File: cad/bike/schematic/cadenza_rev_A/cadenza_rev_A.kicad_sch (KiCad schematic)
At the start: 49 parts, among them J1 USB_A, J2 USB_C_Receptacle, J3 Conn_01x02, J4 Conn_01x02, Q1 BC547, U1 TLC5916, U10 HDSP-A151, U11 TLC5916, U12 HDSP-A151, U13 STM32F105RCTx, U15 TLC5916, U2 HDSP-A151, U3 TLC5916, U4 HDSP-A151, U5 TLC5916, U6 HDSP-A151, U7 TLC5916, U8 HDSP-A151, U9 TLC5916

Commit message: added the 3.3V LDO + switches + push buttons
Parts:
- added C13: 10nF, Capacitor_SMD:C_0805_2012Metric_Pad1.18x1.45mm_HandSolder, symbol Device:C
- added D10: LED, LED_THT:LED_D3.0mm, symbol Device:LED
- added H1, H2, H3, H4: MountingHole_Pad, MountingHole:MountingHole_3.2mm_M3_Pad_Via, symbol Mechanical:MountingHole_Pad
- added J5: Conn_01x02, Connector_PinHeader_2.54mm:PinHeader_1x02_P2.54mm_Vertical, symbol Connector_Generic:Conn_01x02
- added R11, R7: R_US, Resistor_SMD:R_0805_2012Metric_Pad1.20x1.40mm_HandSolder, symbol Device:R_US
- added SW1: SW_Slide_DPDT, Button_Switch_THT:SW_NKK_GW12LJP, symbol Switch:SW_Slide_DPDT
- added SW2, SW3: SW_Push, Button_Switch_SMD:SW_Push_1P1T_NO_CK_KSC6xxG, symbol Switch:SW_Push
- added U14: LT1962-3.3, Package_SO:MSOP-8_3x3mm_P0.65mm, symbol Regulator_Linear:LT1962-3.3
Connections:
- net +3.3V: now also C13.1, J5.1 (Pin_1), U14.1 (OUT), U14.2 (SENSE)
- net +5V: now also R11.1, U14.5 (~{SHDN}), U14.8 (IN)
- net GND: now also J2.S1 (SHIELD), D10.1 (K), H1.1, H2.1, H3.1, H4.1, R7.2, U14.4 (GND)
- net at J2.A4 (VBUS), J2.A9 (VBUS), J2.B4 (VBUS)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: now also SW1.2 (B); no longer J4.1 (Pin_1)
- new net: J4.1 (Pin_1), SW1.3 (C)
- new net: C13.2, U14.3 (BYP)
- new net: J5.2 (Pin_2), R7.1
- new net: D10.2 (A), R11.2
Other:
- moved on the sheet: C1, C10, C11, C2, C9, D9, J1, J2, J4, R5, U13

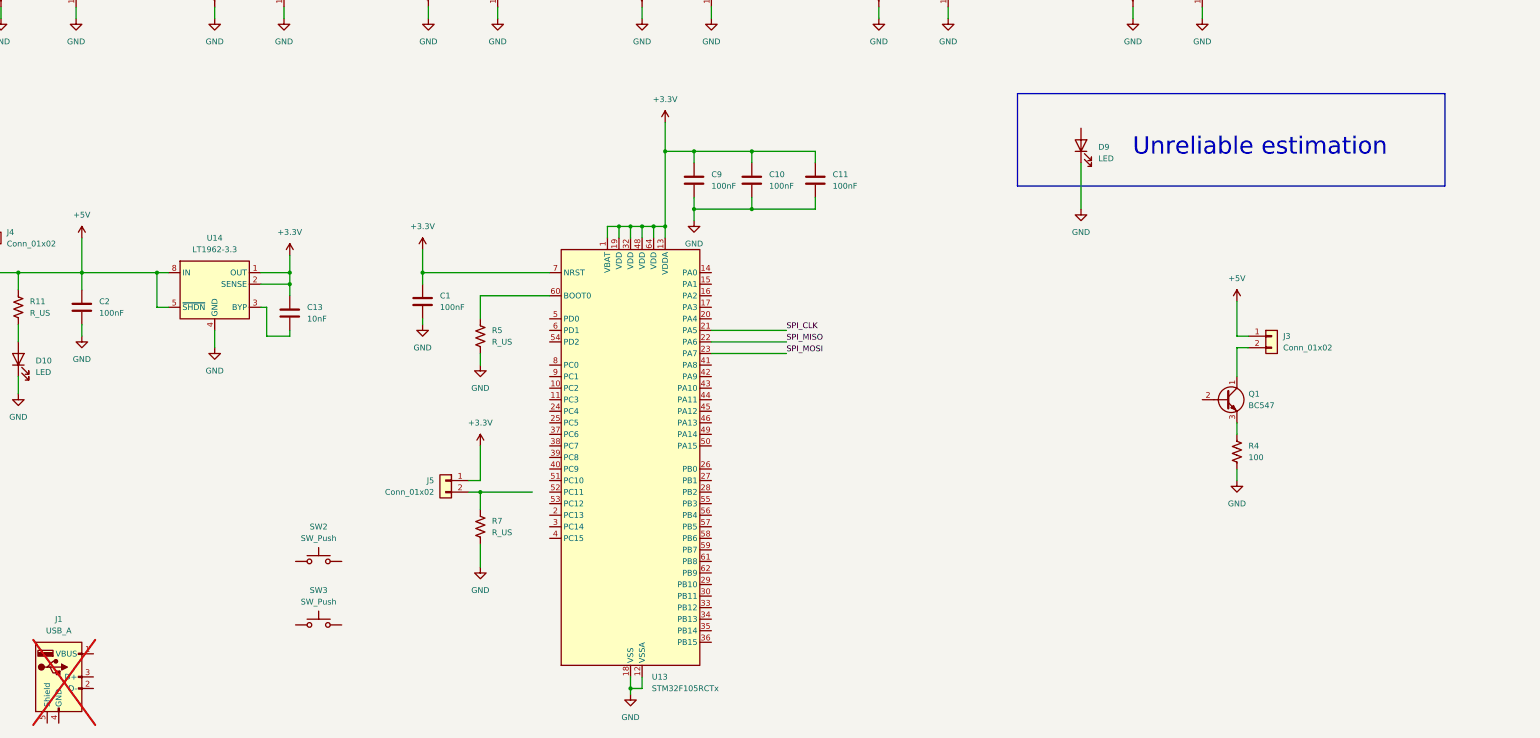
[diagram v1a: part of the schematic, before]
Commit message: added the debug interface
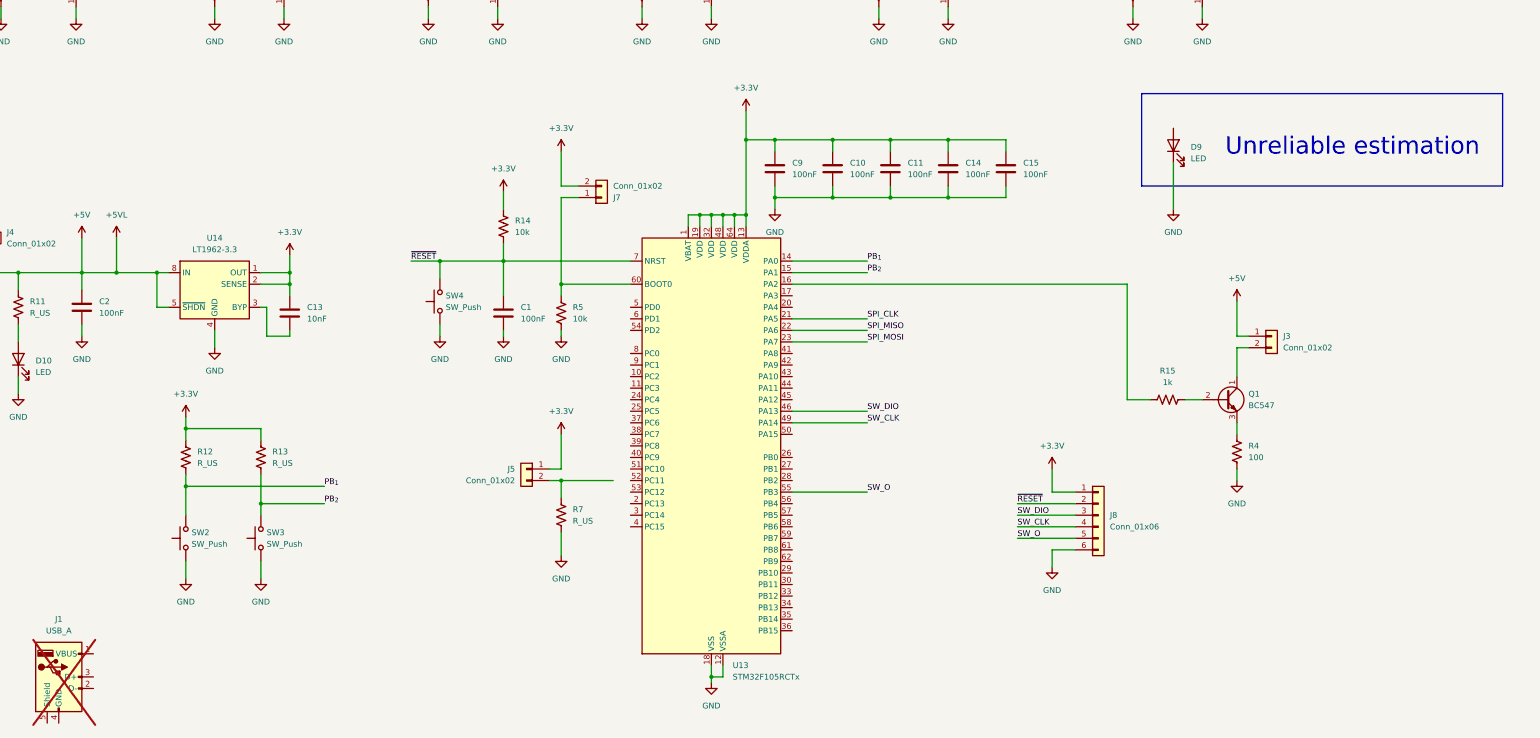
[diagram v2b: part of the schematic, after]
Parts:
- added C14, C15: 100nF, Capacitor_SMD:C_0805_2012Metric_Pad1.18x1.45mm_HandSolder, symbol Device:C
- added J7: Conn_01x02, Connector_PinHeader_2.54mm:PinHeader_1x02_P2.54mm_Vertical, symbol Connector_Generic:Conn_01x02
- added J8: Conn_01x06, Connector_PinHeader_2.54mm:PinHeader_1x06_P2.54mm_Vertical, symbol Connector_Generic:Conn_01x06
- added R12, R13: R_US, Resistor_SMD:R_0805_2012Metric_Pad1.20x1.40mm_HandSolder, symbol Device:R_US
- added R14: 10k, Resistor_SMD:R_0805_2012Metric_Pad1.20x1.40mm_HandSolder, symbol Device:R_US
- added R15: 1k, Resistor_SMD:R_0805_2012Metric_Pad1.20x1.40mm_HandSolder, symbol Device:R_US
- added SW4: SW_Push, Button_Switch_SMD:SW_Push_1P1T_NO_CK_KSC6xxG, symbol Switch:SW_Push
- R5: value R_US -> 10k
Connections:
- net +5VL is gone; now on net +5V: D1.2 (A), D2.2 (A), D3.2 (A), D4.2 (A), D5.2 (A), D6.2 (A), D7.2 (A), D8.2 (A), U10.1 (CA), U10.6 (CA), U12.1 (CA), U12.6 (CA), U2.1 (CA), U2.6 (CA), U4.1 (CA), U4.6 (CA), U6.1 (CA), U6.6 (CA), U8.1 (CA), U8.6 (CA)
- net +3.3V: now also C14.1, C15.1, J7.2 (Pin_2), J8.1 (Pin_1), R12.1, R13.1, R14.1; no longer C1.1, U13.7 (NRST)
- net GND: now also SW2.1, SW3.1, C14.2, C15.2, J8.6 (Pin_6), SW4.1
- net PB_{2}: now reaches SW3.2
- net PB_{2}: now also U13.15 (PA1), R13.2
- net PB_{1}: now reaches U13.14 (PA0)
- net PB_{1}: now also SW2.2, R12.2
- net at U13.16 (PA2): now also R15.1
- net SW_DIO: now reaches U13.46 (PA13)
- net SW_DIO: now also J8.3 (Pin_3)
- net SW_CLK: now reaches U13.49 (PA14)
- net SW_CLK: now also J8.4 (Pin_4)
- net SW_O: now reaches U13.55 (PB3)
- net SW_O: now also J8.5 (Pin_5)
- net at R5.1, U13.60 (BOOT0): now also J7.1 (Pin_1)
- net at Q1.2 (B): now also R15.2
- new net ~{RESET}: C1.1, J8.2 (Pin_2), R14.2, SW4.2, U13.7 (NRST)
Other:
- moved on the sheet: C1, C10, C11, C9, D9, J5, R5, R7, SW2, SW3, U13

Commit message: routing backup
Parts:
- added C16, C17, C18, C19: 100nF, Capacitor_SMD:C_0805_2012Metric_Pad1.18x1.45mm_HandSolder, symbol Device:C
- added R16: 330, Resistor_SMD:R_0805_2012Metric_Pad1.20x1.40mm_HandSolder, symbol Device:R_US
- R12, R13, R7: value R_US -> 4.7k
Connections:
- net +3.3V: now also R7.1, C19.1; no longer J5.1 (Pin_1)
- net GND: now also C16.2, C17.2, C18.2, C19.2; no longer R7.2
- net PB_{1}: now also C16.1
- net PB_{2}: now also C17.1
- net at J2.A4 (VBUS), J2.A9 (VBUS), J2.B4 (VBUS)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: now also SW1.5 (B); no longer SW1.2 (B)
- net at SW1.3 (C): no longer J4.1 (Pin_1)
- net at SW1.6 (C): now also J4.1 (Pin_1)
- net ~{LED_OUTPUT_EN}: now reaches U1.13 (~{OE}(ED2)), U11.13 (~{OE}(ED2)), U15.13 (~{OE}(ED2)), U3.13 (~{OE}(ED2)), U5.13 (~{OE}(ED2)), U7.13 (~{OE}(ED2)), U9.13 (~{OE}(ED2))
- net ~{LED_OUTPUT_EN}: now also U13.35 (PB14)
- net LED_LATCH_EN: now reaches U1.4 (LE(ED1)), U11.4 (LE(ED1)), U15.4 (LE(ED1)), U3.4 (LE(ED1)), U5.4 (LE(ED1)), U7.4 (LE(ED1)), U9.4 (LE(ED1))
- net LED_LATCH_EN: now also U13.20 (PA4)
- net WARNING_LED: now reaches U13.33 (PB12)
- net WARNING_LED: now also R16.1
- net at U13.40 (PC9): now also J5.2 (Pin_2), C18.1
- net at D9.2 (A): now also R16.2
- new net: J5.1 (Pin_1), R7.2
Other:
- note added: "sensor input"
- moved on the sheet: C12, C3, C4, C5, C6, C7, C8, D1, D2, D3, D4, D5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

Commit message: added final touches, no more nets to route
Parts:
- added TP1, TP2, TP3, TP4, TP5: TestPoint, TestPoint:TestPoint_Pad_D1.0mm, symbol Connector:TestPoint
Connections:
- net LED_LATCH_EN: now also TP3.1
- net SPI_CLK: now also TP1.1
- net SPI_MISO: now also TP5.1
- net SPI_MOSI: now also TP2.1
- net ~{LED_OUTPUT_EN}: now also TP4.1
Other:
- moved on the sheet: SW1

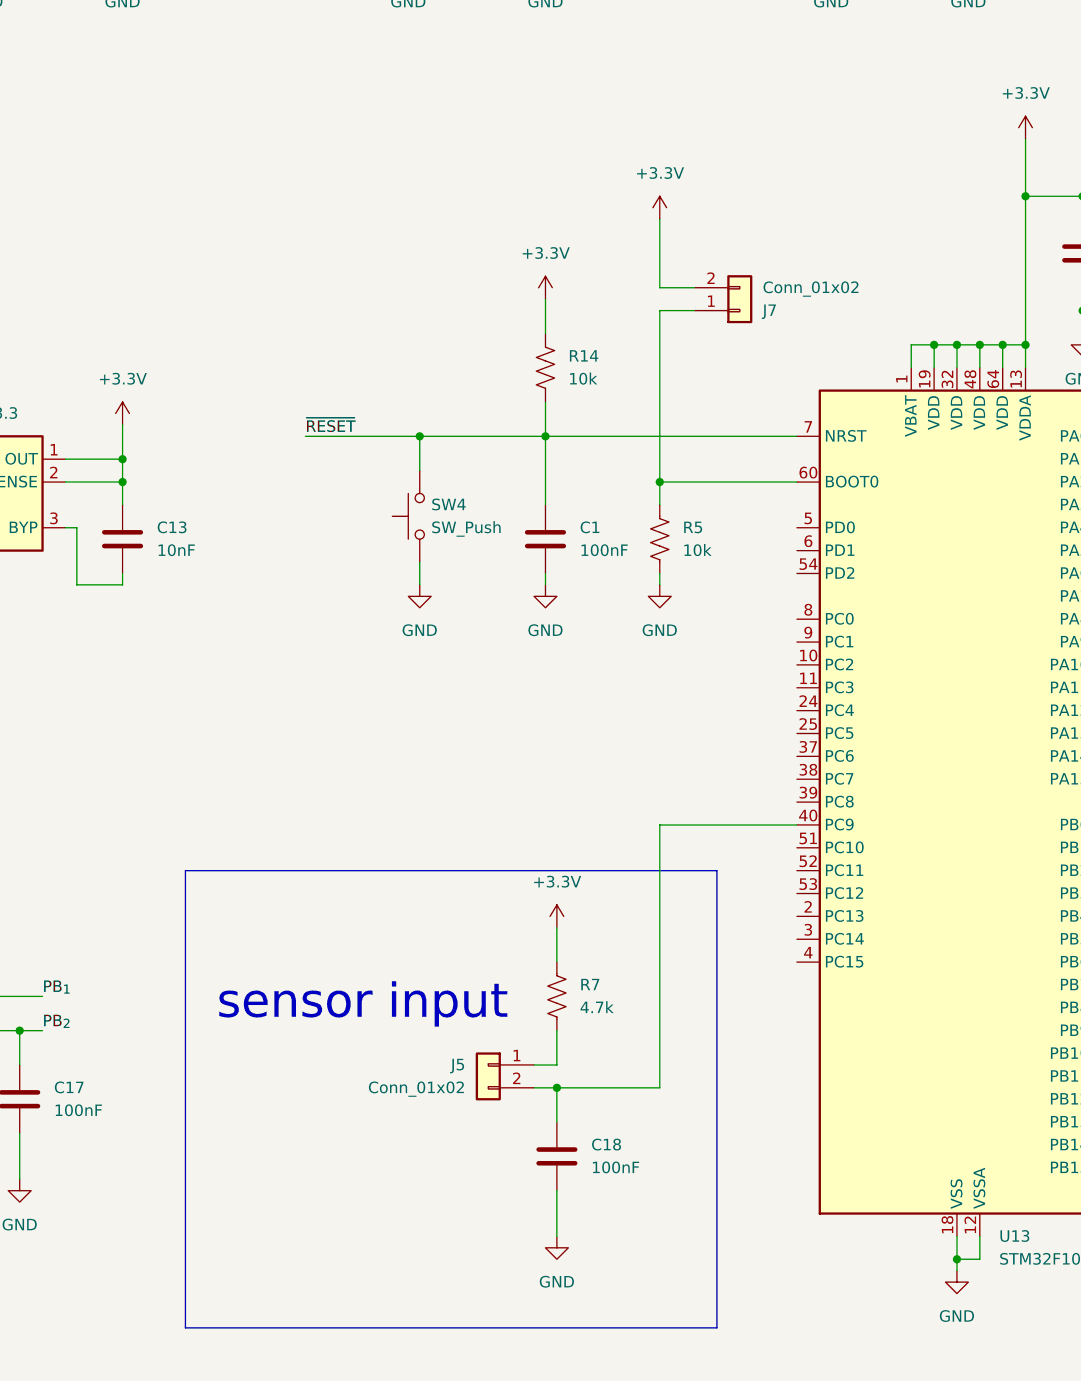
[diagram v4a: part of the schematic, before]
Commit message: added schematic added software pinout definition
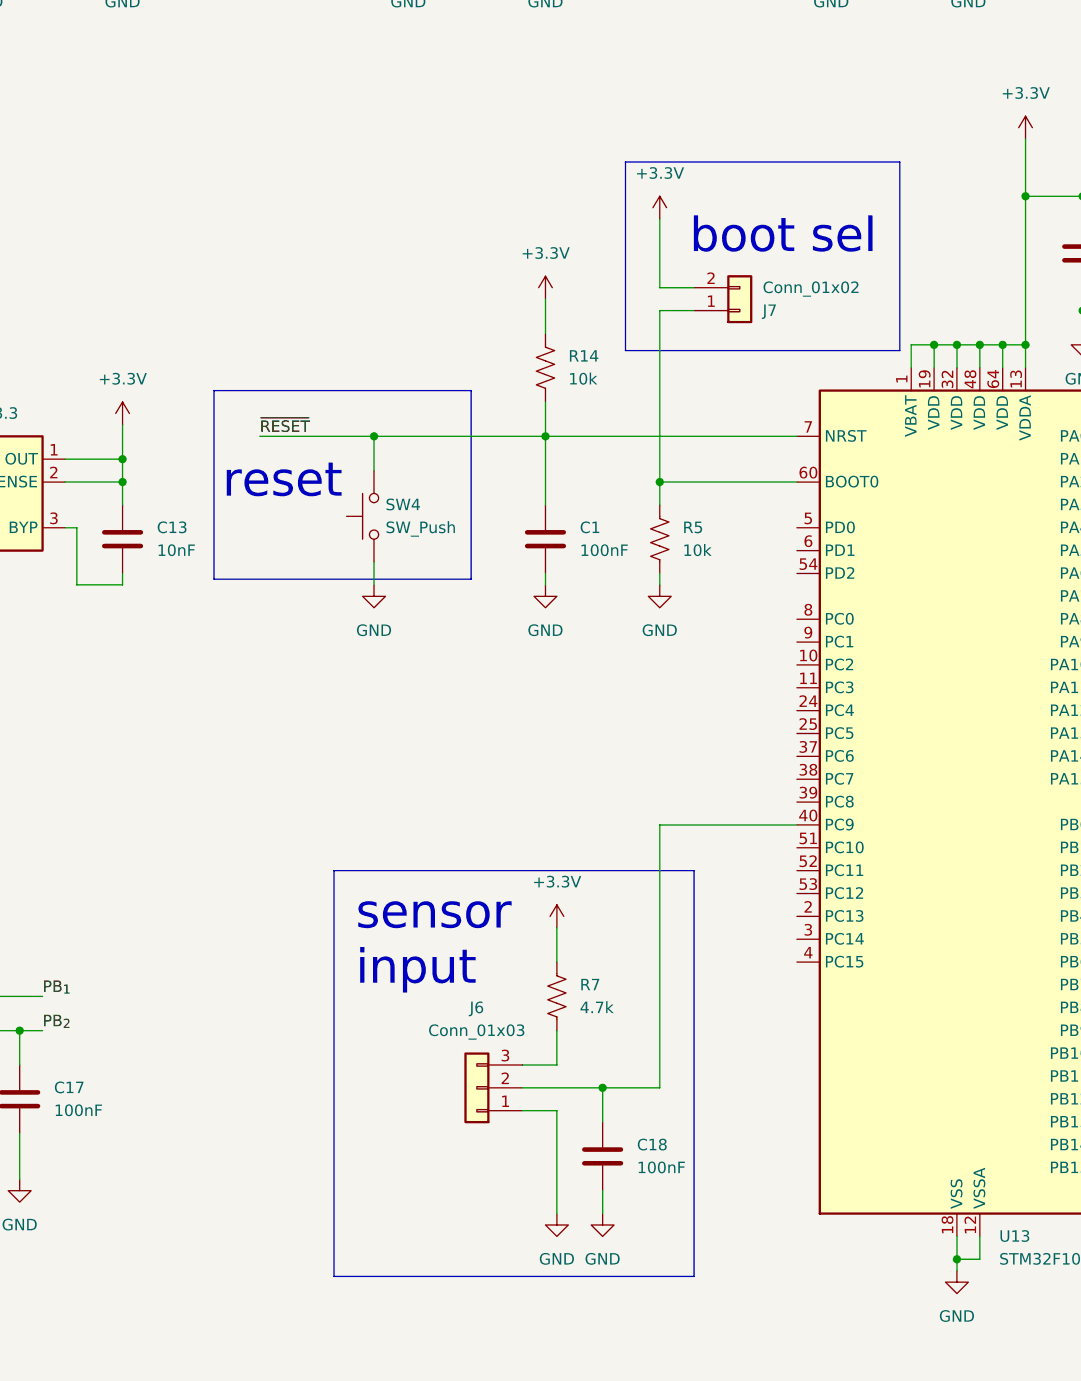
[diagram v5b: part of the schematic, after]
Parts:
- removed J5: Conn_01x02, Connector_PinHeader_2.54mm:PinHeader_1x02_P2.54mm_Vertical, symbol Connector_Generic:Conn_01x02
- added J6: Conn_01x03, Connector_PinHeader_2.54mm:PinHeader_1x03_P2.54mm_Vertical, symbol Connector_Generic:Conn_01x03
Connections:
- net GND: now also J6.1 (Pin_1)
- net at C18.1, U13.40 (PC9): now also J6.2 (Pin_2)
- net at R7.2: now also J6.3 (Pin_3)
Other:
- note added: "boot sel"
- note added: "reset"
- moved on the sheet: C18, SW4
